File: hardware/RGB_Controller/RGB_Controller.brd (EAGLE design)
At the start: 53.8 x 55.5 mm, 19 parts, among them IC1 7805TV, J1 J5MM, J2 J5MM, J3 J5MM, Q1 IRF520, Q2 IRF520, Q3 IRF520

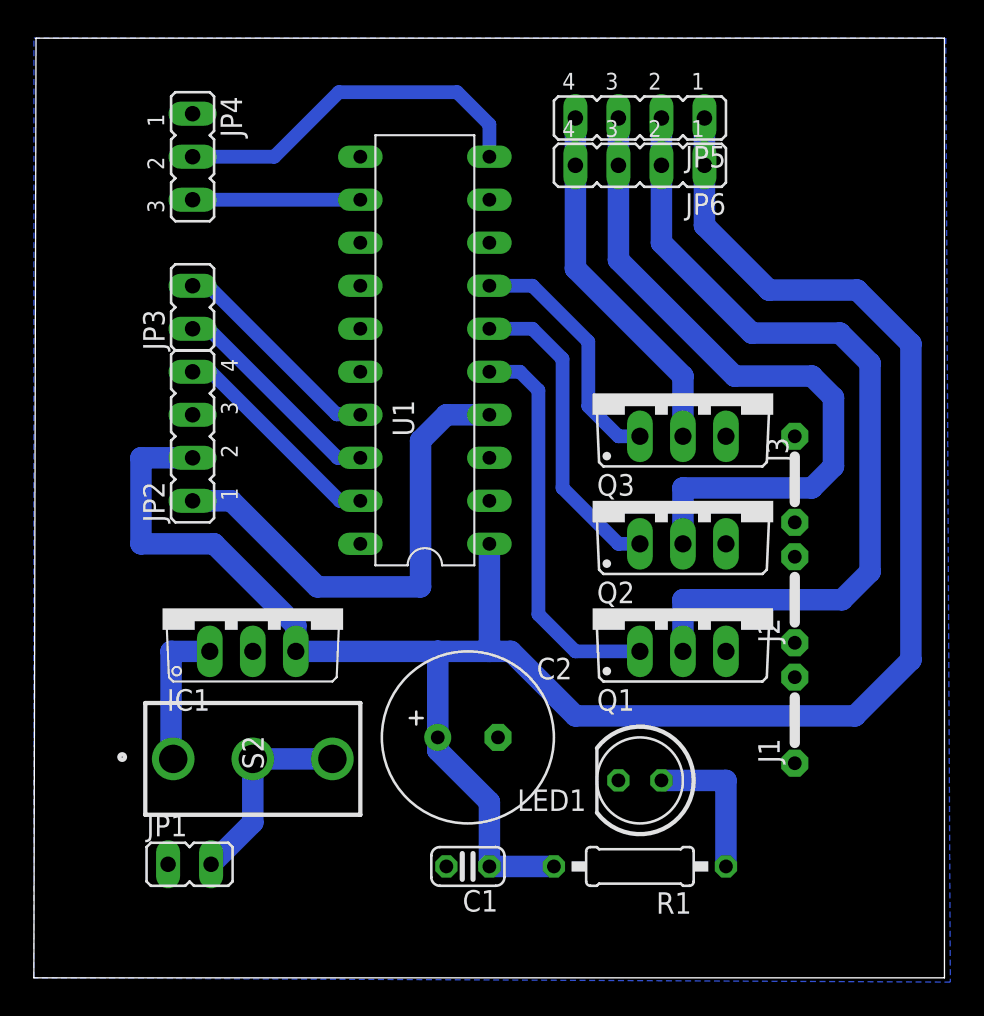
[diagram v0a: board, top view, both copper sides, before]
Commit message: Fixed Colour Inconsistency
- Changed flushOutput() from serial to flush() function
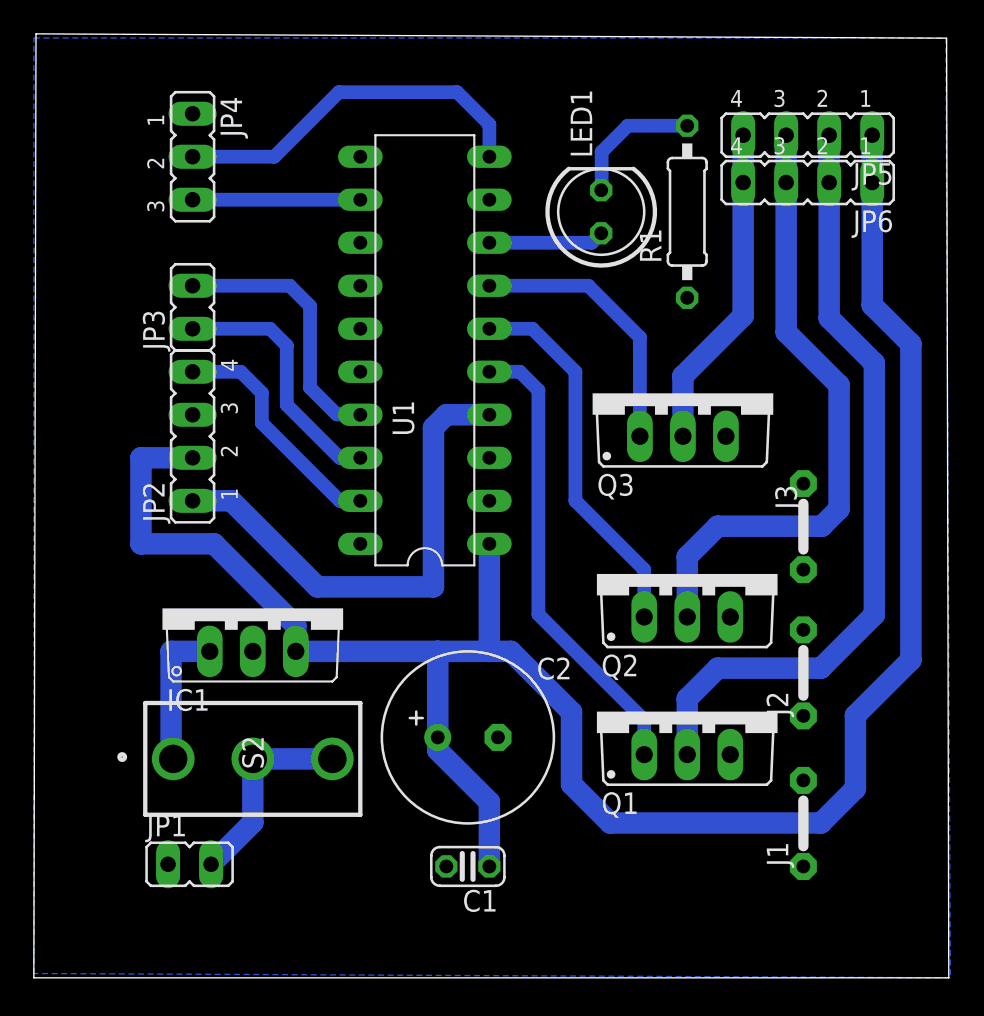
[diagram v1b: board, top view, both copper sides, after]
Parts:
- moved R1 38.8 mm to (38.6, 45.2), turned to 90 degrees
- moved LED1 33.7 mm to (33.5, 45.2), turned to 90 degrees
- moved JP6 9.96 mm to (45.7, 47.0)
- moved JP5 9.96 mm to (45.7, 49.8)
- moved J1 6.12 mm to (45.4, 9.12)
- moved Q1 6.10 mm to (38.6, 15.7)
- moved J2 4.35 mm to (45.4, 18.0)
- moved Q2 4.33 mm to (38.6, 23.9)
- moved J3 2.84 mm to (45.4, 26.6)
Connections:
- new net N$15: LED1.A, U1.8
- net +5V: no longer R1.2
- net N$3: now also LED1.K, R1.2; no longer LED1.A, R1.1
- net PE: now also R1.1; no longer LED1.K
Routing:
- net N$15: track 0.00 -> 6.84 mm
- net N$13: track 41.2 -> 37.1 mm
- net N$9: track 23.5 -> 27.4 mm
- net N$12: track 49.7 -> 45.8 mm
- net N$10: track 18.6 -> 22.3 mm
- net N$6: track 13.1 -> 15.9 mm
- net N$14: track 21.4 -> 19.3 mm
- net N$5: track 13.1 -> 15.1 mm
- net +5V: track 124.3 -> 122.6 mm
- net N$11: track 14.8 -> 16.0 mm
- net N$4: track 13.1 -> 14.1 mm
- net N$3: track 8.89 -> 7.97 mm
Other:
- board size 53.8 x 55.5 mm -> 54 x 55.7 mm

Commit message: Added Sip Pins
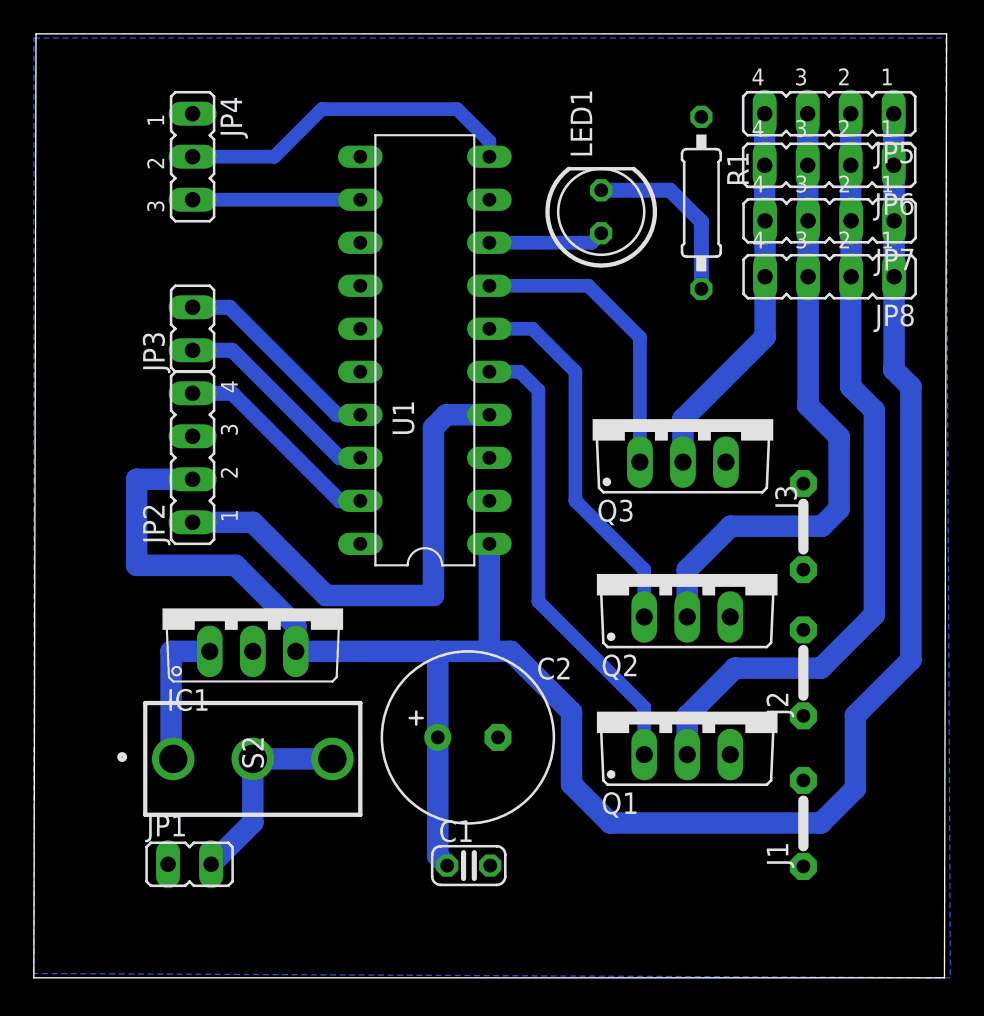
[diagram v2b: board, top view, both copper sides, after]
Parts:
- added JP7, JP8: (no value), jumper:JP4
- moved JP5 1.80 mm to (47.0, 51.0)
- moved JP6 1.63 mm to (47.0, 48.0)
- moved Q3 1.52 mm to (38.3, 33.0)
- moved JP2 1.27 mm to (9.37, 30.7)
- moved JP3 1.27 mm to (9.37, 38.3)
- moved R1 0.99 mm to (39.4, 45.8), turned to 270 degrees
- moved C1 0.07 mm to (25.7, 6.63), turned to 0 degrees
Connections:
- net +5V: now also JP7.1, JP8.1
- net N$12: now also JP7.2, JP8.2
- net N$13: now also JP7.3, JP8.3
- net N$14: now also JP7.4, JP8.4
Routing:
- net N$6: track 15.9 -> 12.5 mm
- net N$14: track 19.3 -> 22.6 mm
- net N$3: track 7.97 -> 10.7 mm
- net N$5: track 15.1 -> 12.5 mm
- net N$4: track 14.1 -> 12.5 mm
- net N$11: track 16.0 -> 17.5 mm
- net N$7: track 21.8 -> 20.4 mm
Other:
- board size 54 x 55.7 mm -> 53.9 x 55.7 mm
